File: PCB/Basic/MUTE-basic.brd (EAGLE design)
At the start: 72.4 x 44.4 mm, 29 parts, among them IC1 REG1117, U1 SILICON_LABS-MICROCONTROLLER-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

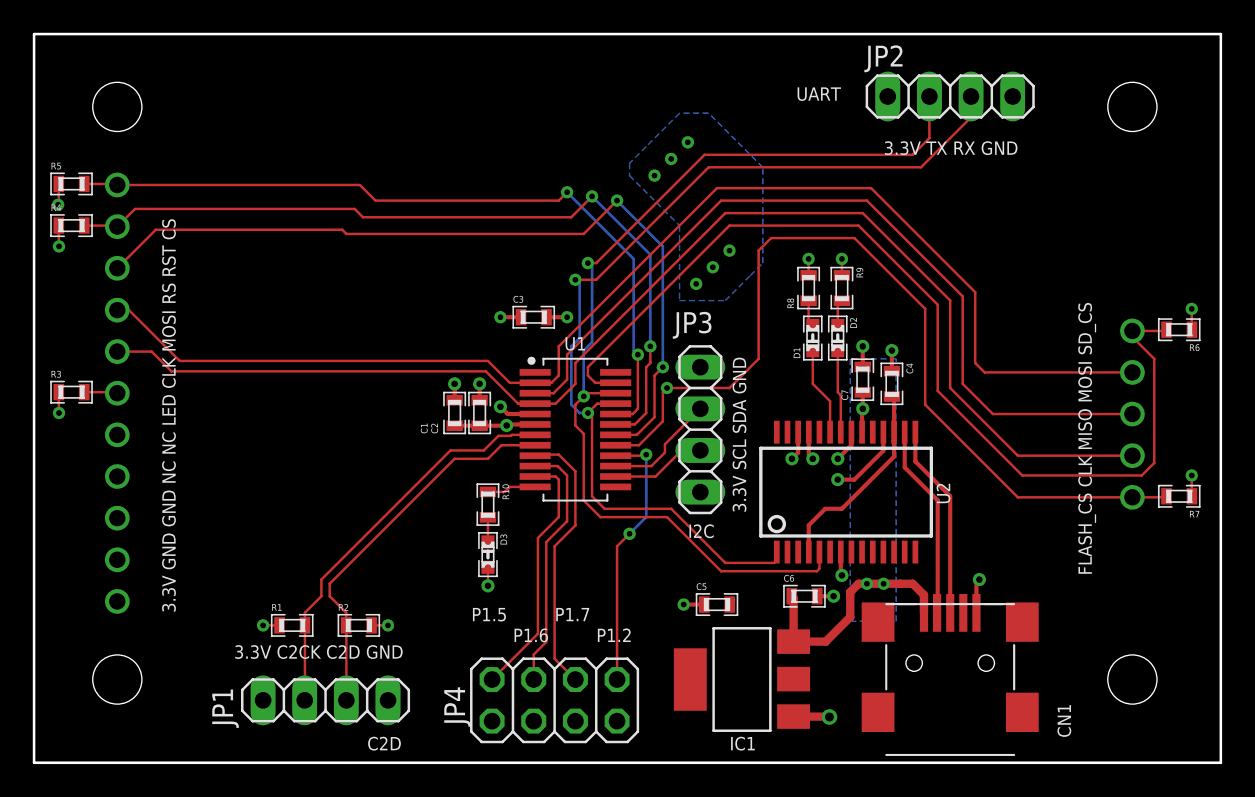
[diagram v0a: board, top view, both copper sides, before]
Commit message: Updated MCU to SOIC16 version for availability
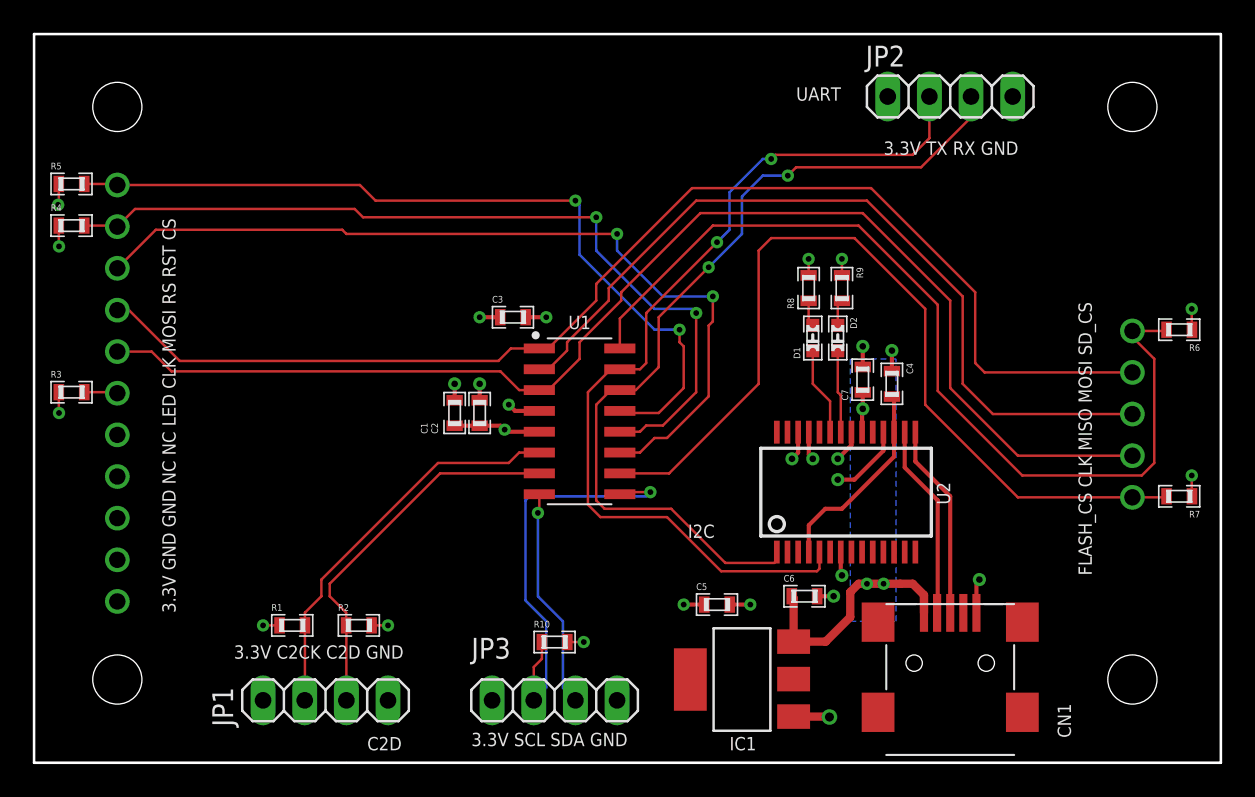
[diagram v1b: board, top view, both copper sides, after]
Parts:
- removed D3: White, standardparts:0603.LED
- removed JP4: (no value), pinhead:2X04
- R10: value 270R -> 4.7k
- U1: value SILICON_LABS-MICROCONTROLLER-EFM8BB1X -> SILICON_LABS-MICROCONTROLLER-EFM8BB10F8G-SOIC16; device Module_ICs:SILICON_LABS-MICROCONTROLLER-EFM8BB10F8G-A-QSOP24R -> Module_ICs:SILICON_LABS-MICROCONTROLLER-EFM8BB10F8G-A-SOIC16
- moved JP3 18.8 mm to (26.7, -1.27), turned to 0 degrees
- moved R10 9.32 mm to (26.7, 2.29), turned to 180 degrees
- moved C3 1.27 mm to (24.1, 22.1)
- moved U1 0.57 mm to (28.2, 15.7)
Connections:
- removed net N$1: D3.P$1, R10.2
- removed net N$10: JP4.2, U1.11
- removed net N$12: JP4.4, U1.10
- removed net N$3: JP4.8, U1.16
- removed net N$5: JP4.6, U1.9
- removed net TEST_LED: R10.1, U1.12
- net C2CK: now also U1.6; no longer U1.7
- net C2D: now also U1.7; no longer U1.8
- net FLASH_CS: now also U1.10; no longer U1.17
- net LCD_CS: now also U1.13; no longer U1.20
- net LCD_SPI_RS: now also U1.11; no longer U1.18
- net LCD_SPI_RST: now also U1.12; no longer U1.19
- net SCL: now also R10.2, U1.9; no longer U1.15
- net SDA: now also U1.8; no longer U1.14
- net SD_CS: now also U1.16; no longer U1.23
- net SPI_CLK: now also U1.3; no longer U1.4
- net SPI_MISO: now also U1.2; no longer U1.3
- net SPI_MOSI: now also U1.1; no longer U1.2
- net UART_RX_MCU_IN: now also U1.14; no longer U1.21
- net UART_TX_MCU_OUT: now also U1.15; no longer U1.22
- net VCC_3V3_IO: now also R10.1, U1.5; no longer JP4.1, JP4.3, U1.6
- net VSS: now also U1.4; no longer D3.P$2, JP4.5, JP4.7, U1.5
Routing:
- net SCL: track 6.91 -> 26.5 mm, vias 0 -> 1
- net N$5: track 16.7 -> 0.00 mm
- net N$3: track 16.3 -> 0.00 mm, vias 2 -> 0
- net N$12: track 15.5 -> 0.00 mm
- net N$10: track 15.4 -> 0.00 mm
- net SDA: track 5.82 -> 13.6 mm, vias 0 -> 1
- net UART_RX_MCU_IN: track 59.3 -> 53.5 mm
- net UART_TX_MCU_OUT: track 61.0 -> 56.7 mm
- net SD_CS: track 60.9 -> 57.2 mm
- net LCD_CS: track 46.6 -> 50.0 mm
- net TEST_LED: track 3.00 -> 0.00 mm
- net LCD_SPI_RST: track 49.1 -> 52.1 mm
- net LCD_SPI_RS: track 49.8 -> 52.6 mm
- net VCC_3V3_IO: track 14.6 -> 17.2 mm, vias 15 -> 11
- net SPI_MOSI: track 76.9 -> 75.3 mm
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- removed copper zone on layer 16, net VCC_3V3_IO
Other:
- board text removed: "P1.2"
- board text removed: "P1.5"
- board text removed: "P1.6"
- board text removed: "P1.7"
